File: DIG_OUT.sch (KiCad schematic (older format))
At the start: 0 parts

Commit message: Testing and adjustments
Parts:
- added D?: LED, symbol Device:LED
- added D?: D, symbol Device:D
- added R? (x2): 4.7k, symbol Device:R_US
- added U?: PC817, Package_DIP:DIP-4_W7.62mm, symbol Isolator:PC817
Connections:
- net labels added: 24V, GND, IN, OUT
- wire segments 0 -> 18
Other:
- note added: "Status LED"
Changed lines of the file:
@@
 $Descr A4 11693 8268
 encoding utf-8
-Sheet 7 7
+Sheet 7 8
 Title "Digital Output"
 Date "2021-05-26"
@@
 Comment4 ""
 $EndDescr
+Text HLabel 4200 3950 0    50   Input ~ 0
+IN
+$Comp
+L Device:LED D?
+U 1 1 60BD3DAF
+P 4650 4200
+AR Path="/60B28EA9/60BD3DAF" Ref="D?"  Part="1"
+AR Path="/60BBF151/60BD3DAF" Ref="D?"  Part="1"
+F 0 "D?" V 4689 4082 50  0000 R CNN
+F 1 "LED" V 4598 4082 50  0000 R CNN
+F 2 "" H 4650 4200 50  0001 C CNN
+F 3 "~" H 4650 4200 50  0001 C CNN
+	1    4650 4200
+	0    -1   -1   0
+$EndComp
+$Comp
+L Device:R_US R?
+U 1 1 60BD3DB5
+P 4650 4600
+AR Path="/60B28EA9/60BD3DB5" Ref="R?"  Part="1"
+AR Path="/60BBF151/60BD3DB5" Ref="R?"  Part="1"
+F 0 "R?" H 4582 4554 50  0000 R CNN
+F 1 "4.7k" H 4582 4645 50  0000 R CNN
+F 2 "" V 4690 4590 50  0001 C CNN
+F 3 "~" H 4650 4600 50  0001 C CNN
+	1    4650 4600
+	-1   0    0    1
+$EndComp
+$Comp
+L Isolator:PC817 U?
+U 1 1 60BD3DBB
+P 6000 4400
+AR Path="/60AC3F67/60BD3DBB" Ref="U?"  Part="1"
+AR Path="/60B28EA9/60BD3DBB" Ref="U?"  Part="1"
+AR Path="/60BBF151/60BD3DBB" Ref="U?"  Part="1"
+F 0 "U?" H 6000 4725 50  0000 C CNN
+F 1 "PC817" H 6000 4634 50  0000 C CNN
+F 2 "Package_DIP:DIP-4_W7.62mm" H 5800 4200 50  0001 L CIN
+F 3 "http://www.soselectronic.cz/a_info/resource/d/pc817.pdf" H 6000 4400 50  0001 L CNN
+	1    6000 4400
+	1    0    0    -1
+$EndComp
+Wire Wire Line
+	5700 3950 5700 4300
+Wire Wire Line
+	5700 4850 5700 4500
+Wire Wire Line
+	4200 3950 4650 3950
+$Comp
+L Device:R_US R?
+U 1 1 60BD3DC4
+P 5150 4850
+AR Path="/60B28EA9/60BD3DC4" Ref="R?"  Part="1"
+AR Path="/60BBF151/60BD3DC4" Ref="R?"  Part="1"
+F 0 "R?" V 4945 4850 50  0000 C CNN
+F 1 "4.7k" V 5036 4850 50  0000 C CNN
+F 2 "" V 5190 4840 50  0001 C CNN
+F 3 "~" H 5150 4850 50  0001 C CNN
+	1    5150 4850
+	0    1    1    0
+$EndComp
+Wire Wire Line
+	4200 4850 4650 4850
+Wire Wire Line
+	4650 4750 4650 4850
+Connection ~ 4650 4850
+Wire Wire Line
+	4650 4850 5000 4850
+Wire Wire Line
+	4650 4450 4650 4350
+Wire Wire Line
+	4650 4050 4650 3950
+Text GLabel 6500 4800 3    50   Input ~ 0
+GND
+Wire Wire Line
+	6300 4300 6500 4300
+Text GLabel 6500 4100 1    50   Input ~ 0
+24V
+Wire Wire Line
+	6300 4500 6350 4500
+Wire Wire Line
+	6350 4500 6350 4550
+Text HLabel 7450 4500 2    50   Input ~ 0
+OUT
+Text Notes 4100 4450 0    50   ~ 0
+Status LED
+Wire Notes Line
+	4550 4050 4950 4050
+Wire Notes Line
+	4950 4050 4950 4750
+Wire Notes Line
+	4950 4750 4550 4750
+Wire Notes Line
+	4550 4750 4550 4050
+$Comp
+L Device:D D?
+U 1 1 60BD3DEC
+P 5500 4400
+AR Path="/60B28EA9/60BD3DEC" Ref="D?"  Part="1"
+AR Path="/60BBF151/60BD3DEC" Ref="D?"  Part="1"
+F 0 "D?" V 5454 4480 50  0000 L CNN
+F 1 "D" V 5545 4480 50  0000 L CNN
+F 2 "" H 5500 4400 50  0001 C CNN
+F 3 "~" H 5500 4400 50  0001 C CNN
+	1    5500 4400
+	0    1    1    0
+$EndComp
+Wire Wire Line
+	4650 3950 5500 3950
+Connection ~ 4650 3950
+Wire Wire Line
+	5700 4850 5500 4850
+Wire Wire Line
+	5500 4550 5500 4850
+Connection ~ 5500 4850
+Wire Wire Line
+	5500 4850 5300 4850
+Wire Wire Line
+	5500 4250 5500 3950
+Connection ~ 5500 3950
+Wire Wire Line
+	5500 3950 5700 3950
+Text GLabel 4200 4850 0    50   Input ~ 0
+GND
+Wire Wire Line
+	6500 4100 6500 4300
 $EndSCHEMATC

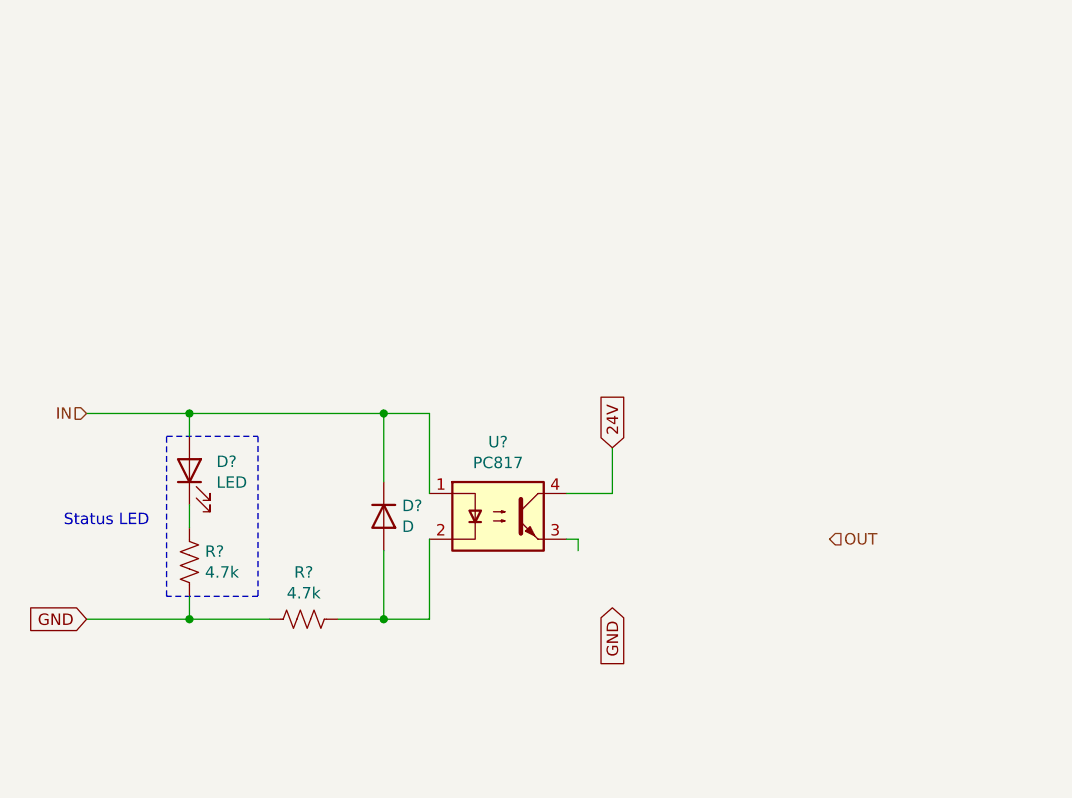
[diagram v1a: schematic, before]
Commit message: Basic Digital Output Circuit (First Revision, UNTESTED)
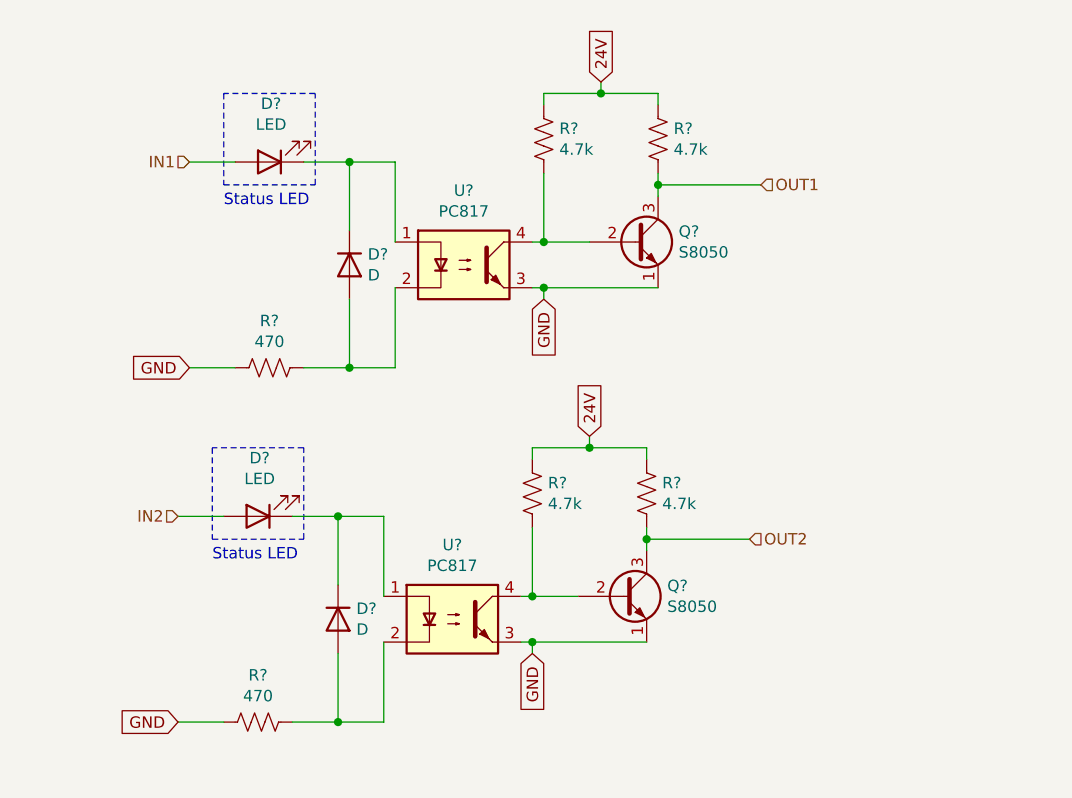
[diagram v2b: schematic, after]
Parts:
- removed D?: LED, symbol Device:LED
- removed D?: D, symbol Device:D
- removed R? (x2): 4.7k, symbol Device:R_US
- removed U?: PC817, Package_DIP:DIP-4_W7.62mm, symbol Isolator:PC817
- added D? (x2): LED, symbol Device:LED
- added D? (x2): D, symbol Device:D
- added Q? (x2): S8050, Package_TO_SOT_THT:TO-92_Inline, symbol Transistor_BJT:S8050
- added R? (x2): 470, symbol Device:R_US
- added R? (x4): 4.7k, symbol Device:R_US
- added U? (x2): PC817, Package_DIP:DIP-4_W7.62mm, symbol Isolator:PC817
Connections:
- net labels added: IN1, IN2, OUT1, OUT2
- net labels removed: IN, OUT
- wire segments 18 -> 48

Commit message: Footprint Association
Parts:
- removed Q? (x2): S8050, Package_TO_SOT_THT:TO-92_Inline, symbol Transistor_BJT:S8050
- added Q2, Q3: BC337, Package_TO_SOT_THT:TO-92_Inline, symbol Transistor_BJT:BC337
- D5, D6: renamed from D?; footprint (none) -> LED_THT:LED_D5.0mm
- D7, D8: renamed from D?; footprint (none) -> Diode_THT:D_A-405_P10.16mm_Horizontal
- R21, R22, R23, R24, R25, R26: renamed from R?; footprint (none) -> Resistor_THT:R_Axial_DIN0207_L6.3mm_D2.5mm_P10.16mm_Horizontal
- gave numbers to parts that had none: 2
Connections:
- net GND: now also Q2.3 (E), Q3.3 (E)
- net OUT1: now also Q3.1 (C)
- net OUT2: now also Q2.1 (C)
- net at R24.2, U8.4: now also Q3.2 (B)
- net at R23.2, U7.4: now also Q2.2 (B)
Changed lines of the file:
@@
 P 5000 2850
 AR Path="/60B28EA9/60C18039" Ref="D?"  Part="1"
-AR Path="/60BBF151/60C18039" Ref="D?"  Part="1"
-F 0 "D?" H 4993 2595 50  0000 C CNN
+AR Path="/60BBF151/60C18039" Ref="D6"  Part="1"
+F 0 "D6" H 4993 2595 50  0000 C CNN
 F 1 "LED" H 4993 2686 50  0000 C CNN
-F 2 "" H 5000 2850 50  0001 C CNN
+F 2 "LED_THT:LED_D5.0mm" H 5000 2850 50  0001 C CNN
 F 3 "~" H 5000 2850 50  0001 C CNN
 	1    5000 2850
@@
 AR Path="/60AC3F67/60C1803F" Ref="U?"  Part="1"
 AR Path="/60B28EA9/60C1803F" Ref="U?"  Part="1"
-AR Path="/60BBF151/60C1803F" Ref="U?"  Part="1"
-F 0 "U?" H 5850 3625 50  0000 C CNN
+AR Path="/60BBF151/60C1803F" Ref="U8"  Part="1"
+F 0 "U8" H 5850 3625 50  0000 C CNN
 F 1 "PC817" H 5850 3534 50  0000 C CNN
 F 2 "Package_DIP:DIP-4_W7.62mm" H 5650 3100 50  0001 L CIN
@@
 P 5000 3750
 AR Path="/60B28EA9/60C18047" Ref="R?"  Part="1"
-AR Path="/60BBF151/60C18047" Ref="R?"  Part="1"
-F 0 "R?" V 4795 3750 50  0000 C CNN
+AR Path="/60BBF151/60C18047" Ref="R22"  Part="1"
+F 0 "R22" V 4795 3750 50  0000 C CNN
 F 1 "470" V 4886 3750 50  0000 C CNN
-F 2 "" V 5040 3740 50  0001 C CNN
+F 2 "Resistor_THT:R_Axial_DIN0207_L6.3mm_D2.5mm_P10.16mm_Horizontal" V 5040 3740 50  0001 C CNN
 F 3 "~" H 5000 3750 50  0001 C CNN
 	1    5000 3750
@@
 P 5350 3300
 AR Path="/60B28EA9/60C18065" Ref="D?"  Part="1"
-AR Path="/60BBF151/60C18065" Ref="D?"  Part="1"
-F 0 "D?" V 5304 3380 50  0000 L CNN
+AR Path="/60BBF151/60C18065" Ref="D8"  Part="1"
+F 0 "D8" V 5304 3380 50  0000 L CNN
 F 1 "D" V 5395 3380 50  0000 L CNN
-F 2 "" H 5350 3300 50  0001 C CNN
+F 2 "Diode_THT:D_A-405_P10.16mm_Horizontal" H 5350 3300 50  0001 C CNN
 F 3 "~" H 5350 3300 50  0001 C CNN
 	1    5350 3300
@@
 Text GLabel 4650 3750 0    50   Input ~ 0
 GND
-$Comp
-L Transistor_BJT:S8050 Q?
-U 1 1 60C18DF6
-P 6600 3200
-F 0 "Q?" H 6790 3246 50  0000 L CNN
-F 1 "S8050" H 6790 3155 50  0000 L CNN
-F 2 "Package_TO_SOT_THT:TO-92_Inline" H 6800 3125 50  0001 L CIN
-F 3 "http://www.unisonic.com.tw/datasheet/S8050.pdf" H 6600 3200 50  0001 L CNN
-	1    6600 3200
-	1    0    0    -1
-$EndComp
 Wire Wire Line
 	6200 3400 6700 3400
@@
 	6150 3200 6200 3200
 $Comp
-L Device:R_US R?
+L Device:R_US R24
 U 1 1 60C19BF3
 P 6200 2750
-F 0 "R?" H 6268 2796 50  0000 L CNN
+F 0 "R24" H 6268 2796 50  0000 L CNN
 F 1 "4.7k" H 6268 2705 50  0000 L CNN
-F 2 "" V 6240 2740 50  0001 C CNN
+F 2 "Resistor_THT:R_Axial_DIN0207_L6.3mm_D2.5mm_P10.16mm_Horizontal" V 6240 2740 50  0001 C CNN
 F 3 "~" H 6200 2750 50  0001 C CNN
 	1    6200 2750
@@
 $EndComp
 $Comp
-L Device:R_US R?
+L Device:R_US R26
 U 1 1 60C1B077
 P 6700 2750
-F 0 "R?" H 6768 2796 50  0000 L CNN
+F 0 "R26" H 6768 2796 50  0000 L CNN
 F 1 "4.7k" H 6768 2705 50  0000 L CNN
-F 2 "" V 6740 2740 50  0001 C CNN
+F 2 "Resistor_THT:R_Axial_DIN0207_L6.3mm_D2.5mm_P10.16mm_Horizontal" V 6740 2740 50  0001 C CNN
 F 3 "~" H 6700 2750 50  0001 C CNN
 	1    6700 2750
@@
 P 4950 4400
 AR Path="/60B28EA9/60C21692" Ref="D?"  Part="1"
-AR Path="/60BBF151/60C21692" Ref="D?"  Part="1"
-F 0 "D?" H 4943 4145 50  0000 C CNN
+AR Path="/60BBF151/60C21692" Ref="D5"  Part="1"
+F 0 "D5" H 4943 4145 50  0000 C CNN
 F 1 "LED" H 4943 4236 50  0000 C CNN
-F 2 "" H 4950 4400 50  0001 C CNN
+F 2 "LED_THT:LED_D5.0mm" H 4950 4400 50  0001 C CNN
 F 3 "~" H 4950 4400 50  0001 C CNN
 	1    4950 4400
@@
 AR Path="/60AC3F67/60C21698" Ref="U?"  Part="1"
 AR Path="/60B28EA9/60C21698" Ref="U?"  Part="1"
-AR Path="/60BBF151/60C21698" Ref="U?"  Part="1"
-F 0 "U?" H 5800 5175 50  0000 C CNN
+AR Path="/60BBF151/60C21698" Ref="U7"  Part="1"
+F 0 "U7" H 5800 5175 50  0000 C CNN
 F 1 "PC817" H 5800 5084 50  0000 C CNN
 F 2 "Package_DIP:DIP-4_W7.62mm" H 5600 4650 50  0001 L CIN
@@
 P 4950 5300
 AR Path="/60B28EA9/60C216A0" Ref="R?"  Part="1"
-AR Path="/60BBF151/60C216A0" Ref="R?"  Part="1"
-F 0 "R?" V 4745 5300 50  0000 C CNN
+AR Path="/60BBF151/60C216A0" Ref="R21"  Part="1"
+F 0 "R21" V 4745 5300 50  0000 C CNN
 F 1 "470" V 4836 5300 50  0000 C CNN
-F 2 "" V 4990 5290 50  0001 C CNN
+F 2 "Resistor_THT:R_Axial_DIN0207_L6.3mm_D2.5mm_P10.16mm_Horizontal" V 4990 5290 50  0001 C CNN
 F 3 "~" H 4950 5300 50  0001 C CNN
 	1    4950 5300
@@
 P 5300 4850
 AR Path="/60B28EA9/60C216AA" Ref="D?"  Part="1"
-AR Path="/60BBF151/60C216AA" Ref="D?"  Part="1"
-F 0 "D?" V 5254 4930 50  0000 L CNN
+AR Path="/60BBF151/60C216AA" Ref="D7"  Part="1"
+F 0 "D7" V 5254 4930 50  0000 L CNN
 F 1 "D" V 5345 4930 50  0000 L CNN
-F 2 "" H 5300 4850 50  0001 C CNN
+F 2 "Diode_THT:D_A-405_P10.16mm_Horizontal" H 5300 4850 50  0001 C CNN
 F 3 "~" H 5300 4850 50  0001 C CNN
 	1    5300 4850
@@
 Text GLabel 4600 5300 0    50   Input ~ 0
 GND
-$Comp
-L Transistor_BJT:S8050 Q?
-U 1 1 60C216BF
-P 6550 4750
-F 0 "Q?" H 6740 4796 50  0000 L CNN
-F 1 "S8050" H 6740 4705 50  0000 L CNN
-F 2 "Package_TO_SOT_THT:TO-92_Inline" H 6750 4675 50  0001 L CIN
-F 3 "http://www.unisonic.com.tw/datasheet/S8050.pdf" H 6550 4750 50  0001 L CNN
-	1    6550 4750
-	1    0    0    -1
-$EndComp
 Wire Wire Line
 	6150 4950 6650 4950
@@
 	6100 4750 6150 4750
 $Comp
-L Device:R_US R?
+L Device:R_US R23
 U 1 1 60C216C8
 P 6150 4300
-F 0 "R?" H 6218 4346 50  0000 L CNN
+F 0 "R23" H 6218 4346 50  0000 L CNN
 F 1 "4.7k" H 6218 4255 50  0000 L CNN
-F 2 "" V 6190 4290 50  0001 C CNN
+F 2 "Resistor_THT:R_Axial_DIN0207_L6.3mm_D2.5mm_P10.16mm_Horizontal" V 6190 4290 50  0001 C CNN
 F 3 "~" H 6150 4300 50  0001 C CNN
 	1    6150 4300
@@
 $EndComp
 $Comp
-L Device:R_US R?
+L Device:R_US R25
 U 1 1 60C216CE
 P 6650 4300
-F 0 "R?" H 6718 4346 50  0000 L CNN
+F 0 "R25" H 6718 4346 50  0000 L CNN
 F 1 "4.7k" H 6718 4255 50  0000 L CNN
-F 2 "" V 6690 4290 50  0001 C CNN
+F 2 "Resistor_THT:R_Axial_DIN0207_L6.3mm_D2.5mm_P10.16mm_Horizontal" V 6690 4290 50  0001 C CNN
 F 3 "~" H 6650 4300 50  0001 C CNN
 	1    6650 4300
@@
 Text HLabel 7100 4500 2    50   Input ~ 0
 OUT2
+$Comp
+L Transistor_BJT:BC337 Q3
+U 1 1 60C43ACA
+P 6600 3200
+F 0 "Q3" H 6791 3246 50  0000 L CNN
+F 1 "BC337" H 6791 3155 50  0000 L CNN
+F 2 "Package_TO_SOT_THT:TO-92_Inline" H 6800 3125 50  0001 L CIN
+F 3 "https://diotec.com/tl_files/diotec/files/pdf/datasheets/bc337.pdf" H 6600 3200 50  0001 L CNN
+	1    6600 3200
+	1    0    0    -1
+$EndComp
+$Comp
+L Transistor_BJT:BC337 Q2
+U 1 1 60C46842
+P 6550 4750
+F 0 "Q2" H 6741 4796 50  0000 L CNN
+F 1 "BC337" H 6741 4705 50  0000 L CNN
+F 2 "Package_TO_SOT_THT:TO-92_Inline" H 6750 4675 50  0001 L CIN
+F 3 "https://diotec.com/tl_files/diotec/files/pdf/datasheets/bc337.pdf" H 6550 4750 50  0001 L CNN
+	1    6550 4750
+	1    0    0    -1
+$EndComp
 $EndSCHEMATC

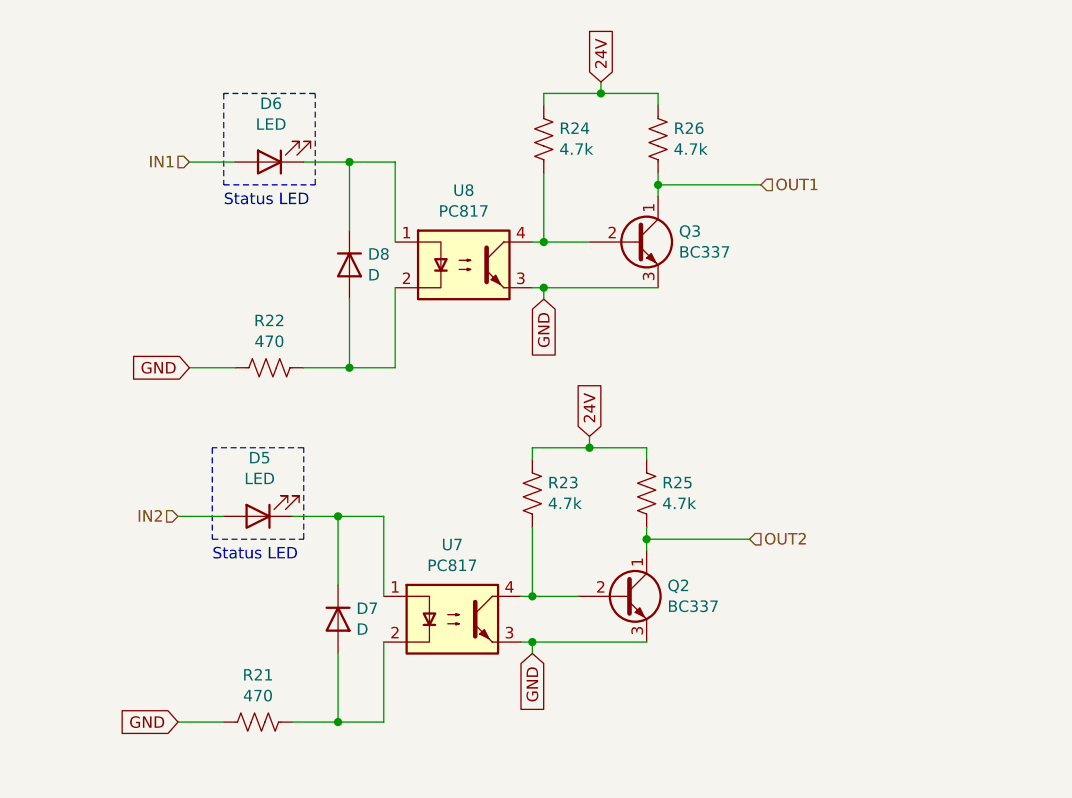
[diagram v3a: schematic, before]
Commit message: Status LED was ruining the reverse voltage protection LED's purpose
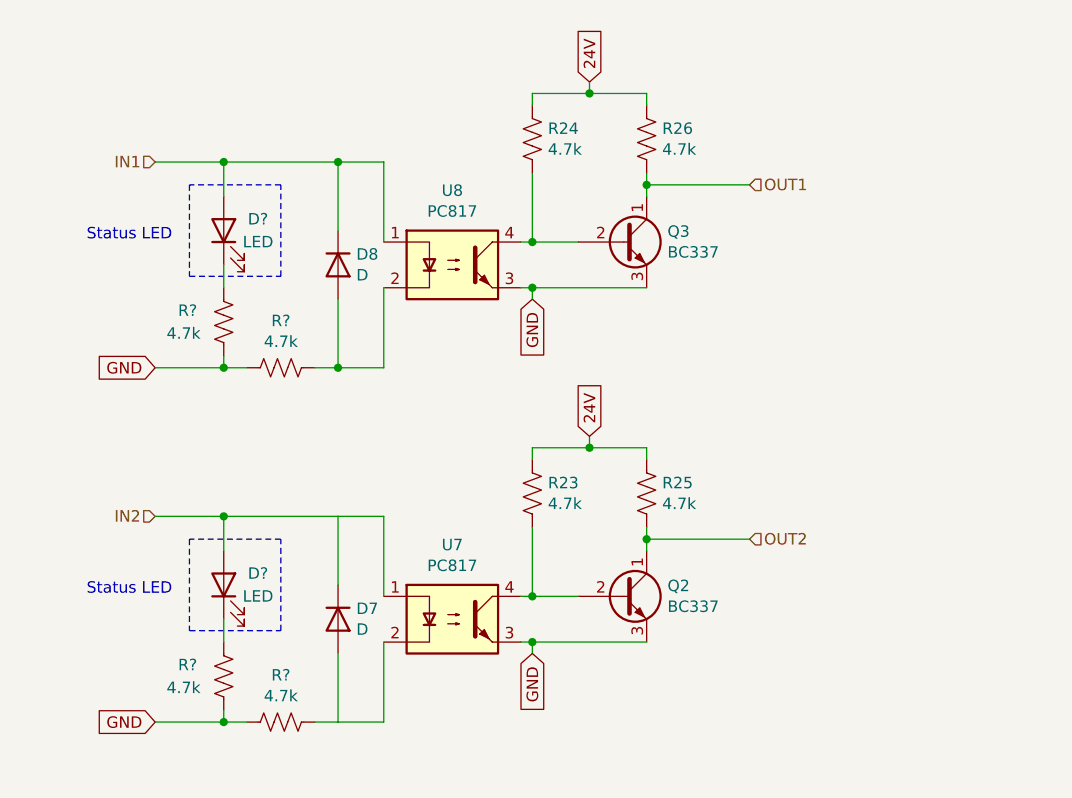
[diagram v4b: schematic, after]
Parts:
- removed D5, D6: LED, LED_THT:LED_D5.0mm, symbol Device:LED
- removed R21, R22: 470, Resistor_THT:R_Axial_DIN0207_L6.3mm_D2.5mm_P10.16mm_Horizontal, symbol Device:R_US
- added D? (x2): LED, LED_THT:LED_D5.0mm, symbol Device:LED
- added R? (x2): 4.7k, Resistor_THT:R_Axial_DIN0207_L6.3mm_D2.5mm_P10.16mm_Horizontal, symbol Device:R_US
- added R? (x2): 4.7k, symbol Device:R_US
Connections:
- net GND: now also R?.1, R?.1, R?.2, R?.2
- net IN1: now also D8.1 (K), U8.1, D?.2 (A)
- net IN2: now also D7.1 (K), U7.1, D?.2 (A)
- net at D8.2 (A), U8.2: now also R?.2
- net at D7.2 (A), U7.2: now also R?.2
- new net: D?.1 (K), R?.1 (x2)
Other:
- moved on the sheet: D8, Q3, R24, R26, U8

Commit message: Finished 1st revision of 24V digital output circuit
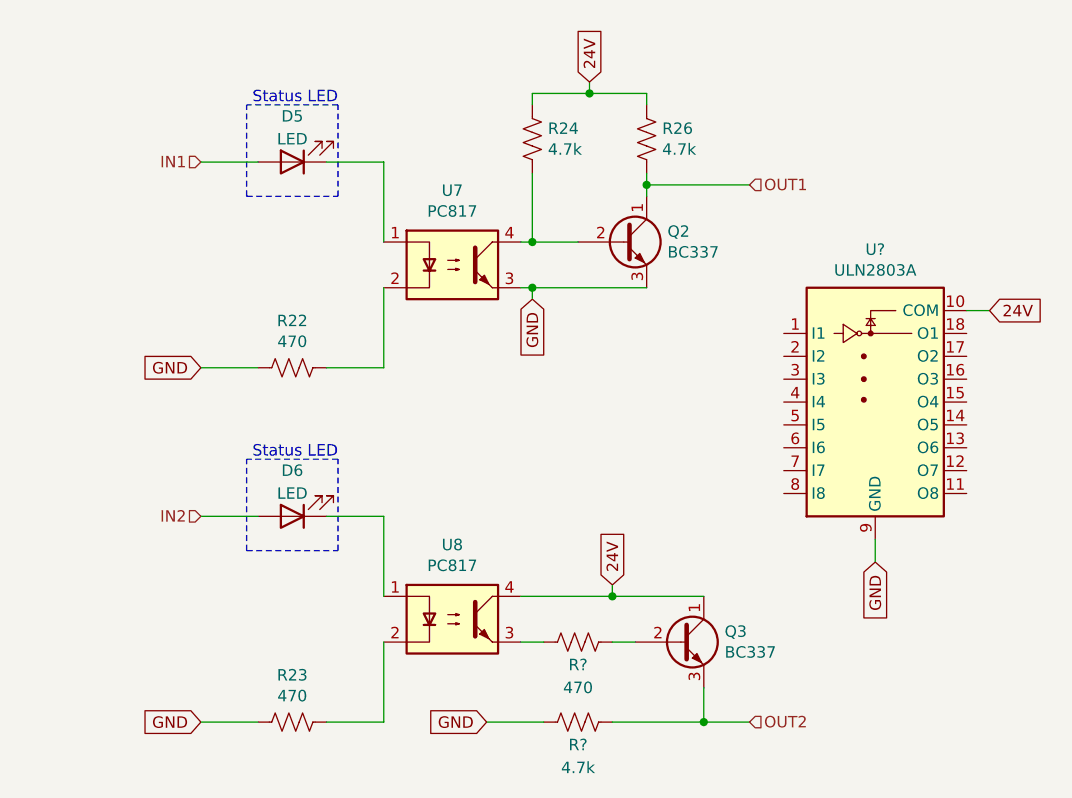
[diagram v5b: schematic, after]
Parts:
- removed D7, D8: D, Diode_THT:D_A-405_P10.16mm_Horizontal, symbol Device:D
- removed D?: LED, LED_THT:LED_D5.0mm, symbol Device:LED
- removed R25, R?: 4.7k, Resistor_THT:R_Axial_DIN0207_L6.3mm_D2.5mm_P10.16mm_Horizontal, symbol Device:R_US
- removed R? (x2): 4.7k, symbol Device:R_US
- added D6: LED, LED_THT:LED_D5.0mm, symbol Device:LED
- added R?: 470, Resistor_THT:R_Axial_DIN0207_L6.3mm_D2.5mm_P10.16mm_Horizontal, symbol Device:R_US
- added R?: 4.7k, Resistor_THT:R_Axial_DIN0207_L6.3mm_D2.5mm_P10.16mm_Horizontal, symbol Device:R_US
- added U?: ULN2803A, symbol Transistor_Array:ULN2803A
- R22: renamed from R?; value 4.7k -> 470
- R23: value 4.7k -> 470
- gave numbers to parts that had none: 1
- renumbered Q3 to Q2, Q2 to Q3, U8 to U7, U7 to U8
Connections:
- net 24V: now also Q3.1 (C), U8.4, U?.10 (COM); no longer R23.1
- net GND: now also R23.1, R?.1, U?.9 (GND); no longer Q3.3 (E), U8.3
- net IN1: no longer U7.1
- net IN2: now also D6.2 (A); no longer U8.1
- net OUT2: now also Q3.3 (E), R?.2; no longer Q3.1 (C)
- net at U8.2: now also R23.2
- net at D5.1 (K): now also U7.1
- new net: D6.1 (K), U8.1
- new net: R?.1, U8.3
- new net: Q3.2 (B), R?.2
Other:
- moved on the sheet: D5, Q3, R22
